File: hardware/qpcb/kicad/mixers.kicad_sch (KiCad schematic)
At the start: 0 parts

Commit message: Add mixer footprint and symbols
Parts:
- added U20, U21, U22: ~, symbol RF_mount_PCBs:mixer
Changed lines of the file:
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@@
 	(generator_version "8.0")
 	(paper "A4")
+	(symbol
+		(lib_id "RF_mount_PCBs:mixer")
+		(at 57.15 62.23 0)
+		(unit 1)
+		(exclude_from_sim no)
+		(in_bom yes)
+		(on_board yes)
+		(dnp no)
+		(fields_autoplaced yes)
+		(property "Reference" "U21"
+			(at 63.5 67.9449 0)
+			(effects
+				(font
+					(size 1.27 1.27)
+				)
+				(justify left)
+			)
+		)
+		(property "Value" "~"
+			(at 63.5 69.85 0)
+			(effects
+				(font
+					(size 1.27 1.27)
+				)
+				(justify left)
+			)
+		)
+		(property "Footprint" ""
+			(at 57.15 62.23 0)
+			(effects
+				(font
+					(size 1.27 1.27)
+				)
+				(hide yes)
+			)
+		)
+		(property "Datasheet" ""
+			(at 57.15 62.23 0)
+			(effects
+				(font
+					(size 1.27 1.27)
+				)
+				(hide yes)
+			)
+		)
+		(property "Description" ""
+			(at 57.15 62.23 0)
+			(effects
+				(font
+					(size 1.27 1.27)
+				)
+				(hide yes)
+			)
+		)
+		(pin "6"
+		)
+		(pin "7"
+		)
+		(pin "2"
+		)
+		(pin "8"
+		)
+		(pin "4"
+		)
+		(pin "5"
+		)
+		(pin "3"
+		)
+		(pin "1"
+		)
+		(instances
+			(project "qpcb"
+				(path "/c131d68b-62f5-4c45-b130-1d10920b3403/0d3fdb9f-aa64-4253-817d-8c2e1f2492e7"
+					(reference "U21")
+					(unit 1)
+				)
+			)
+		)
+	)
+	(symbol
+		(lib_id "RF_mount_PCBs:mixer")
+		(at 57.15 39.37 0)
+		(unit 1)
+		(exclude_from_sim no)
+		(in_bom yes)
+		(on_board yes)
+		(dnp no)
+		(fields_autoplaced yes)
+		(property "Reference" "U20"
+			(at 63.5 45.0849 0)
+			(effects
+				(font
+					(size 1.27 1.27)
+				)
+				(justify left)
+			)
+		)
+		(property "Value" "~"
+			(at 63.5 46.99 0)
+			(effects
+				(font
+					(size 1.27 1.27)
+				)
+				(justify left)
+			)
+		)
+		(property "Footprint" ""
+			(at 57.15 39.37 0)
+			(effects
+				(font
+					(size 1.27 1.27)
+				)
+				(hide yes)
+			)
+		)
+		(property "Datasheet" ""
+			(at 57.15 39.37 0)
+			(effects
+				(font
+					(size 1.27 1.27)
+				)
+				(hide yes)
+			)
+		)
+		(property "Description" ""
+			(at 57.15 39.37 0)
+			(effects
+				(font
+					(size 1.27 1.27)
+				)
+				(hide yes)
+			)
+		)
+		(pin "4"
+		)
+		(pin "3"
+		)
+		(pin "7"
+		)
+		(pin "8"
+		)
+		(pin "1"
+		)
+		(pin "5"
+		)
+		(pin "6"
+		)
+		(pin "2"
+		)
+		(instances
+			(project "qpcb"
+				(path "/c131d68b-62f5-4c45-b130-1d10920b3403/0d3fdb9f-aa64-4253-817d-8c2e1f2492e7"
+					(reference "U20")
+					(unit 1)
+				)
+			)
+		)
+	)
+	(symbol
+		(lib_id "RF_mount_PCBs:mixer")
+		(at 57.15 87.63 0)
+		(unit 1)
+		(exclude_from_sim no)
+		(in_bom yes)
+		(on_board yes)
+		(dnp no)
+		(fields_autoplaced yes)
+		(property "Reference" "U22"
+			(at 63.5 93.3449 0)
+			(effects
+				(font
+					(size 1.27 1.27)
+				)
+				(justify left)
+			)
+		)
+		(property "Value" "~"
+			(at 63.5 95.25 0)
+			(effects
+				(font
+					(size 1.27 1.27)
+				)
+				(justify left)
+			)
+		)
+		(property "Footprint" ""
+			(at 57.15 87.63 0)
+			(effects
+				(font
+					(size 1.27 1.27)
+				)
+				(hide yes)
+			)
+		)
+		(property "Datasheet" ""
+			(at 57.15 87.63 0)
+			(effects
+				(font
+					(size 1.27 1.27)
+				)
+				(hide yes)
+			)
+		)
+		(property "Description" ""
+			(at 57.15 87.63 0)
+			(effects
+				(font
+					(size 1.27 1.27)
+				)
+				(hide yes)
+			)
+		)
+		(pin "1"
+		)
+		(pin "3"
+		)
+		(pin "5"
+		)
+		(pin "6"
+		)
+		(pin "7"
+		)
+		(pin "4"
+		)
+		(pin "2"
+		)
+		(pin "8"
+		)
+		(instances
+			(project "qpcb"
+				(path "/c131d68b-62f5-4c45-b130-1d10920b3403/0d3fdb9f-aa64-4253-817d-8c2e1f2492e7"
+					(reference "U22")
+					(unit 1)
+				)
+			)
+		)
+	)
 )

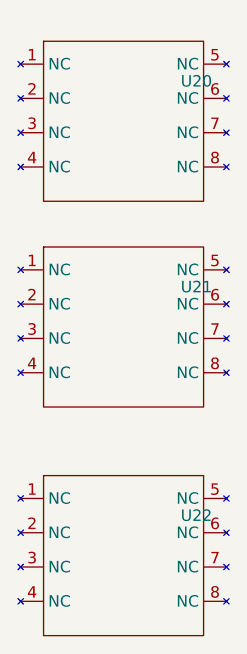
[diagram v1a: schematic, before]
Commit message: Final version of MC43063A and fill components' production info
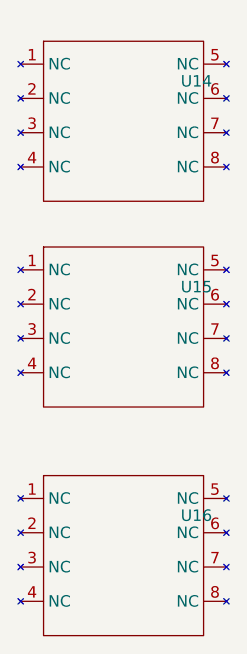
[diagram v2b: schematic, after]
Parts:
- renumbered U20 to U14, U21 to U15, U22 to U16
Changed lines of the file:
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@@
 		(dnp no)
 		(fields_autoplaced yes)
-		(property "Reference" "U21"
+		(property "Reference" "U15"
 			(at 63.5 67.9449 0)
 			(effects
@@
 		)
 		(property "Description" ""
+			(at 57.15 62.23 0)
+			(effects
+				(font
+					(size 1.27 1.27)
+				)
+				(hide yes)
+			)
+		)
+		(property "Manufacturer Part Number" ""
+			(at 57.15 62.23 0)
+			(effects
+				(font
+					(size 1.27 1.27)
+				)
+				(hide yes)
+			)
+		)
+		(property "Field-1" ""
 			(at 57.15 62.23 0)
 			(effects
@@
 			(project "qpcb"
 				(path "/c131d68b-62f5-4c45-b130-1d10920b3403/0d3fdb9f-aa64-4253-817d-8c2e1f2492e7"
-					(reference "U21")
+					(reference "U15")
 					(unit 1)
 				)
@@
 		(dnp no)
 		(fields_autoplaced yes)
-		(property "Reference" "U20"
+		(property "Reference" "U14"
 			(at 63.5 45.0849 0)
 			(effects
@@
 		)
 		(property "Description" ""
+			(at 57.15 39.37 0)
+			(effects
+				(font
+					(size 1.27 1.27)
+				)
+				(hide yes)
+			)
+		)
+		(property "Manufacturer Part Number" ""
+			(at 57.15 39.37 0)
+			(effects
+				(font
+					(size 1.27 1.27)
+				)
+				(hide yes)
+			)
+		)
+		(property "Field-1" ""
 			(at 57.15 39.37 0)
 			(effects
@@
 			(project "qpcb"
 				(path "/c131d68b-62f5-4c45-b130-1d10920b3403/0d3fdb9f-aa64-4253-817d-8c2e1f2492e7"
-					(reference "U20")
+					(reference "U14")
 					(unit 1)
 				)
@@
 		(dnp no)
 		(fields_autoplaced yes)
-		(property "Reference" "U22"
+		(property "Reference" "U16"
 			(at 63.5 93.3449 0)
 			(effects
@@
 		)
 		(property "Description" ""
+			(at 57.15 87.63 0)
+			(effects
+				(font
+					(size 1.27 1.27)
+				)
+				(hide yes)
+			)
+		)
+		(property "Manufacturer Part Number" ""
+			(at 57.15 87.63 0)
+			(effects
+				(font
+					(size 1.27 1.27)
+				)
+				(hide yes)
+			)
+		)
+		(property "Field-1" ""
 			(at 57.15 87.63 0)
 			(effects
@@
 			(project "qpcb"
 				(path "/c131d68b-62f5-4c45-b130-1d10920b3403/0d3fdb9f-aa64-4253-817d-8c2e1f2492e7"
-					(reference "U22")
+					(reference "U16")
 					(unit 1)
 				)

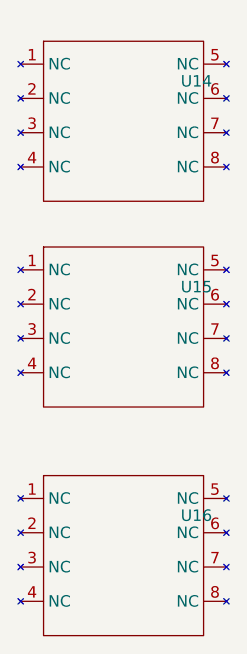
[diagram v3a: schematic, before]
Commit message: Add final footprints of daughter boards, change components for -3v3 power supply line and placement almost finished
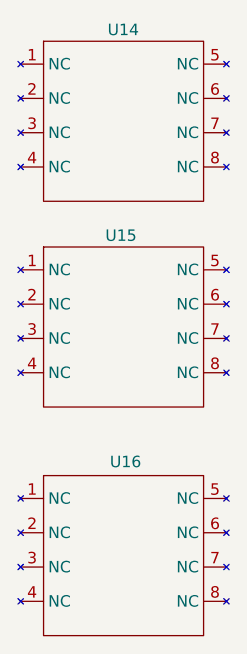
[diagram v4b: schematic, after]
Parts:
- U14, U15, U16: footprint (none) -> footprints:mixer
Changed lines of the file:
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@@
 		(on_board yes)
 		(dnp no)
-		(fields_autoplaced yes)
 		(property "Reference" "U15"
-			(at 63.5 67.9449 0)
+			(at 55.118 62.23 0)
 			(effects
 				(font
@@
 			)
 		)
-		(property "Footprint" ""
+		(property "Footprint" "footprints:mixer"
 			(at 57.15 62.23 0)
 			(effects
@@
 		(on_board yes)
 		(dnp no)
-		(fields_autoplaced yes)
 		(property "Reference" "U14"
-			(at 63.5 45.0849 0)
+			(at 55.372 39.37 0)
 			(effects
 				(font
@@
 			)
 		)
-		(property "Footprint" ""
+		(property "Footprint" "footprints:mixer"
 			(at 57.15 39.37 0)
 			(effects
@@
 		(on_board yes)
 		(dnp no)
-		(fields_autoplaced yes)
 		(property "Reference" "U16"
-			(at 63.5 93.3449 0)
+			(at 55.626 87.376 0)
 			(effects
 				(font
@@
 			)
 		)
-		(property "Footprint" ""
+		(property "Footprint" "footprints:mixer"
 			(at 57.15 87.63 0)
 			(effects
